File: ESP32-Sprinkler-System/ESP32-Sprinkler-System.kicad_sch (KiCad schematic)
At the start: 18 parts, among them J101 12V, J102 DHT, J103 NEOPIXEL, J104 LCD, J105 BME280, U101 V7805-500, U102 ESP32-DEVKITC-32D

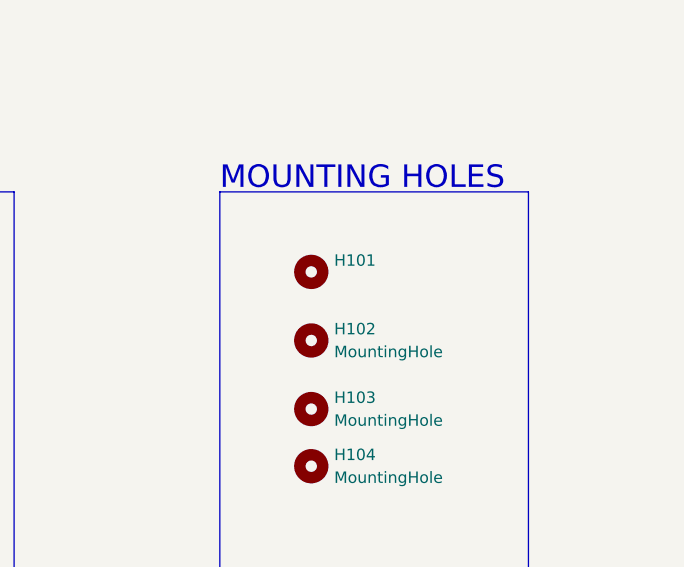
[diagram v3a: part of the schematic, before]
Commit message: Added comments to PCB in UserComments layer.
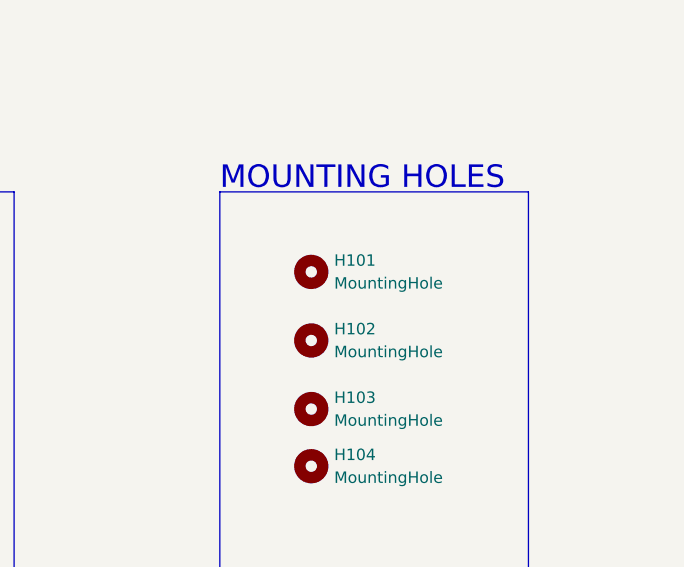
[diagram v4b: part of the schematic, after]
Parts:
- H101: value (none) -> MountingHole; footprint (none) -> MountingHole:MountingHole_3.2mm_M3
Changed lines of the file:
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@@
       (effects (font (size 1.27 1.27)) (justify left))
     )
-    (property "Value" "" (id 1) (at 241.3 48.2599 0)
+    (property "Value" "MountingHole" (id 1) (at 241.3 48.2599 0)
       (effects (font (size 1.27 1.27)) (justify left))
     )
-    (property "Footprint" "" (id 2) (at 238.76 46.99 0)
+    (property "Footprint" "MountingHole:MountingHole_3.2mm_M3" (id 2) (at 238.76 46.99 0)
       (effects (font (size 1.27 1.27)) hide)
     )
